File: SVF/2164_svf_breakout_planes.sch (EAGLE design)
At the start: 88 parts, among them IC1 SSM2164P, IC2 TL072, IC3 TL072, IC4 TL072, IC5 TL072, IC6 TL072, U1 THONKICONNNEW, U2 THONKICONNNEW, U3 THONKICONNNEW, U4 THONKICONNNEW, U5 THONKICONNNEW, U6 THONKICONNNEW

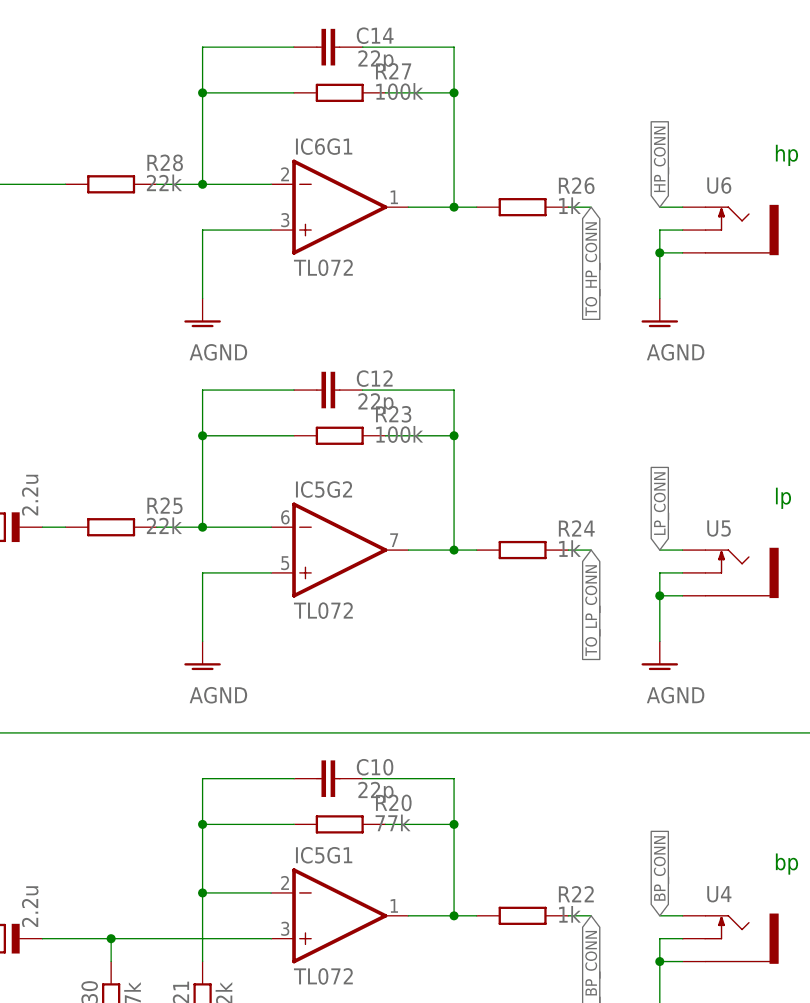
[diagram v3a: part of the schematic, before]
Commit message: Trim output gains for more conservative levels
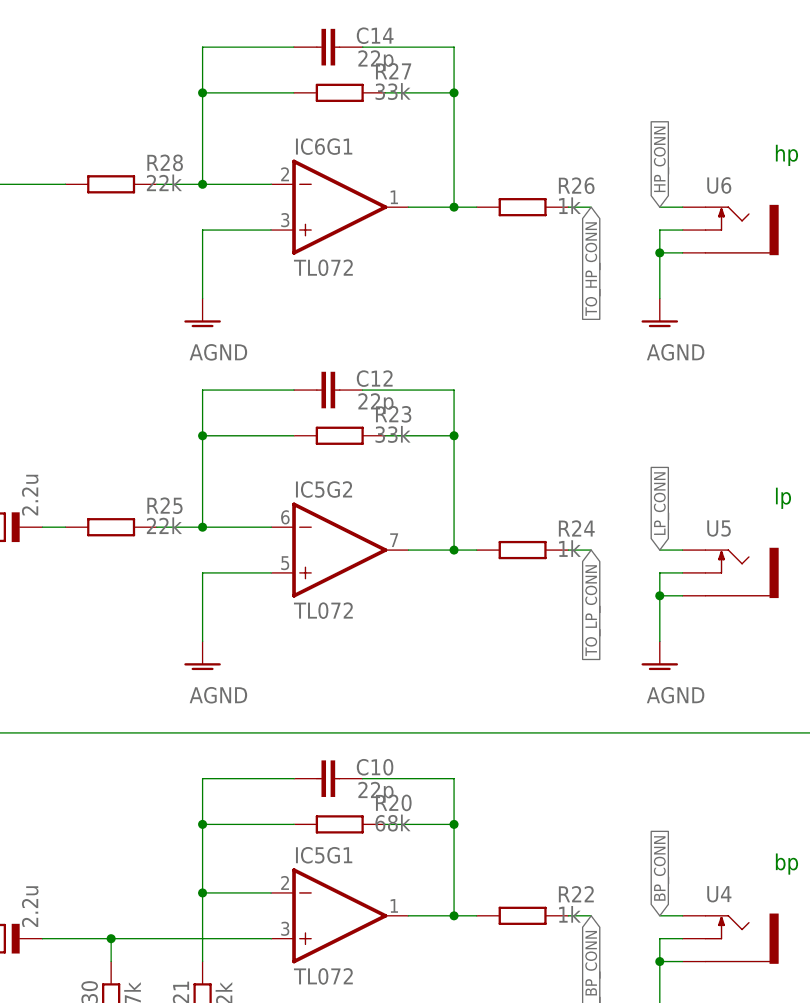
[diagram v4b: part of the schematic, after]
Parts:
- R20: value 77k -> 68k
- R23, R27: value 100k -> 33k
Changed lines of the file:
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@@
 <part name="IC5" library="SparkFun-IC-Amplifiers" library_urn="urn:adsk.eagle:library:520" deviceset="OPAMP-DUAL" device="" package3d_urn="urn:adsk.eagle:package:38666/1" technology="DIP" value="TL072"/>
 <part name="IC6" library="SparkFun-IC-Amplifiers" library_urn="urn:adsk.eagle:library:520" deviceset="OPAMP-DUAL" device="" package3d_urn="urn:adsk.eagle:package:38666/1" technology="DIP" value="TL072"/>
-<part name="R20" library="rcl" library_urn="urn:adsk.eagle:library:334" deviceset="R-EU_" device="0207/2V" package3d_urn="urn:adsk.eagle:package:23490/1" value="77k"/>
+<part name="R20" library="rcl" library_urn="urn:adsk.eagle:library:334" deviceset="R-EU_" device="0207/2V" package3d_urn="urn:adsk.eagle:package:23490/1" value="68k"/>
 <part name="R21" library="rcl" library_urn="urn:adsk.eagle:library:334" deviceset="R-EU_" device="0207/2V" package3d_urn="urn:adsk.eagle:package:23490/1" value="22k"/>
 <part name="R22" library="rcl" library_urn="urn:adsk.eagle:library:334" deviceset="R-EU_" device="0207/2V" package3d_urn="urn:adsk.eagle:package:23490/1" value="1k"/>
@@
 <part name="AGND19" library="supply1" library_urn="urn:adsk.eagle:library:371" deviceset="AGND" device=""/>
 <part name="AGND20" library="supply1" library_urn="urn:adsk.eagle:library:371" deviceset="AGND" device=""/>
-<part name="R23" library="rcl" library_urn="urn:adsk.eagle:library:334" deviceset="R-EU_" device="0207/2V" package3d_urn="urn:adsk.eagle:package:23490/1" value="100k"/>
+<part name="R23" library="rcl" library_urn="urn:adsk.eagle:library:334" deviceset="R-EU_" device="0207/2V" package3d_urn="urn:adsk.eagle:package:23490/1" value="33k"/>
 <part name="C12" library="rcl" library_urn="urn:adsk.eagle:library:334" deviceset="C-EU" device="050-025X075" package3d_urn="urn:adsk.eagle:package:23637/1" value="22p"/>
 <part name="R24" library="rcl" library_urn="urn:adsk.eagle:library:334" deviceset="R-EU_" device="0207/2V" package3d_urn="urn:adsk.eagle:package:23490/1" value="1k"/>
@@
 <part name="U6" library="MusicThingModular" deviceset="THONKICONN" device="NEW" override_package3d_urn="urn:adsk.eagle:package:27955746/2" override_package_urn="urn:adsk.eagle:footprint:27955747/1"/>
 <part name="AGND23" library="supply1" library_urn="urn:adsk.eagle:library:371" deviceset="AGND" device=""/>
-<part name="R27" library="rcl" library_urn="urn:adsk.eagle:library:334" deviceset="R-EU_" device="0207/2V" package3d_urn="urn:adsk.eagle:package:23490/1" value="100k"/>
+<part name="R27" library="rcl" library_urn="urn:adsk.eagle:library:334" deviceset="R-EU_" device="0207/2V" package3d_urn="urn:adsk.eagle:package:23490/1" value="33k"/>
 <part name="C14" library="rcl" library_urn="urn:adsk.eagle:library:334" deviceset="C-EU" device="050-025X075" package3d_urn="urn:adsk.eagle:package:23637/1" value="22p"/>
 <part name="R28" library="rcl" library_urn="urn:adsk.eagle:library:334" deviceset="R-EU_" device="0207/2V" package3d_urn="urn:adsk.eagle:package:23490/1" value="22k"/>

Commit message: Add V1.7 files for SVF
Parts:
- added D7: BAT85, diode:SCHOTTKY-DIODEDO35-7
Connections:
- net AGND: now also D7.C
- net V-: now also D7.A
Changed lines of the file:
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@@
 <part name="R30" library="rcl" library_urn="urn:adsk.eagle:library:334" deviceset="R-EU_" device="0207/2V" package3d_urn="urn:adsk.eagle:package:23490/1" value="17k"/>
 <part name="AGND39" library="supply1" library_urn="urn:adsk.eagle:library:371" deviceset="AGND" device=""/>
+<part name="D7" library="diode" library_urn="urn:adsk.eagle:library:210" deviceset="SCHOTTKY-DIODE" device="DO35-7" package3d_urn="urn:adsk.eagle:package:43339/2" value="BAT85"/>
 </parts>
 <sheets>
@@
 <text x="279.4" y="236.22" size="1.778" layer="91">hp</text>
 <text x="246.38" y="50.8" size="1.778" layer="91">resonance</text>
-<text x="86.36" y="175.26" size="1.778" layer="91">cutoff</text>
+<text x="81.28" y="177.8" size="1.778" layer="91">cutoff</text>
 <text x="38.1" y="93.98" size="1.778" layer="91">input</text>
 <text x="40.64" y="132.08" size="1.778" layer="91">cv1</text>
@@
 <attribute name="VALUE" x="312.42" y="124.46" size="1.778" layer="96" rot="R180"/>
 </instance>
-<instance part="AGND32" gate="VR1" x="30.48" y="193.04" smashed="yes">
-<attribute name="VALUE" x="35.56" y="190.5" size="1.778" layer="96" rot="R180"/>
+<instance part="AGND32" gate="VR1" x="30.48" y="180.34" smashed="yes">
+<attribute name="VALUE" x="35.56" y="177.8" size="1.778" layer="96" rot="R180"/>
 </instance>
 <instance part="AGND33" gate="VR1" x="127" y="12.7" smashed="yes">
@@
 <instance part="AGND39" gate="VR1" x="205.74" y="129.54" smashed="yes">
 <attribute name="VALUE" x="210.82" y="127" size="1.778" layer="96" rot="R180"/>
+</instance>
+<instance part="D7" gate="G$1" x="45.72" y="198.12" smashed="yes" rot="MR90">
+<attribute name="NAME" x="47.625" y="195.834" size="1.778" layer="95" rot="MR90"/>
+<attribute name="VALUE" x="42.291" y="195.834" size="1.778" layer="96" rot="MR90"/>
 </instance>
 </instances>
@@
 <wire x1="25.4" y1="203.2" x2="30.48" y2="203.2" width="0.1524" layer="91"/>
 <pinref part="AGND32" gate="VR1" pin="AGND"/>
-<wire x1="30.48" y1="203.2" x2="30.48" y2="195.58" width="0.1524" layer="91"/>
+<wire x1="30.48" y1="203.2" x2="30.48" y2="182.88" width="0.1524" layer="91"/>
 <pinref part="C28" gate="G$1" pin="2"/>
 <pinref part="C27" gate="G$1" pin="1"/>
@@
 <wire x1="30.48" y1="205.74" x2="30.48" y2="203.2" width="0.1524" layer="91"/>
 <junction x="30.48" y="203.2"/>
+<pinref part="D7" gate="G$1" pin="C"/>
+<wire x1="45.72" y1="200.66" x2="45.72" y2="205.74" width="0.1524" layer="91"/>
+<wire x1="45.72" y1="205.74" x2="38.1" y2="205.74" width="0.1524" layer="91"/>
 </segment>
 <segment>
@@
 <wire x1="38.1" y1="187.96" x2="17.78" y2="187.96" width="0.1524" layer="91"/>
 <junction x="17.78" y="187.96"/>
-</segment>
-</net>
+<wire x1="38.1" y1="187.96" x2="45.72" y2="187.96" width="0.1524" layer="91"/>
+<junction x="38.1" y="187.96"/>
+<pinref part="D7" gate="G$1" pin="A"/>
+<wire x1="45.72" y1="187.96" x2="45.72" y2="195.58" width="0.1524" layer="91"/>
+</segment>
+</net>
